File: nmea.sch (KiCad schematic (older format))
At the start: 24 parts, among them P7 CONN_01X20, U7 MCP2562, U8 SN65C1168E, U9 INA219

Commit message: More renaming from bb to kbox
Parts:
- P7: footprint bb:TerminalBlock_Pheonix_PT-3.5mm_20pol -> kbox:TerminalBlock_Pheonix_PT-3.5mm_20pol
- U7, U9: footprint bb:SOIC8N -> kbox:SOIC8N
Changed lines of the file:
@@
 EESchema Schematic File Version 2
-LIBS:bb
+LIBS:kbox
 LIBS:power
 LIBS:device
@@
 LIBS:w_device
 LIBS:gsg-symbols
-LIBS:bb1-cache
+LIBS:kbox-cache
 EELAYER 25 0
 EELAYER END
@@
 F 0 "U7" H 2900 1550 60  0000 C CNN
 F 1 "MCP2562" H 2850 2050 60  0000 C CNN
-F 2 "bb:SOIC8N" H 2900 1750 60  0001 C CNN
+F 2 "kbox:SOIC8N" H 2900 1750 60  0001 C CNN
 F 3 "" H 2900 1750 60  0000 C CNN
 F 4 "MCP2562T-E/SN" H 2900 1850 60  0001 C CNN "PartNumber"
@@
 F 0 "U9" H 3400 4950 60  0000 C CNN
 F 1 "INA219" H 3100 4950 60  0000 C CNN
-F 2 "bb:SOIC8N" H 3200 4700 60  0001 C CNN
+F 2 "kbox:SOIC8N" H 3200 4700 60  0001 C CNN
 F 3 "" H 3200 4700 60  0000 C CNN
 F 4 "INA219BIDR" H 3200 4700 60  0001 C CNN "PartNumber"
@@
 F 0 "P7" H 9350 5800 50  0000 C CNN
 F 1 "CONN_01X20" V 9450 4750 50  0000 C CNN
-F 2 "bb:TerminalBlock_Pheonix_PT-3.5mm_20pol" H 9350 4750 60  0001 C CNN
+F 2 "kbox:TerminalBlock_Pheonix_PT-3.5mm_20pol" H 9350 4750 60  0001 C CNN
 F 3 "" H 9350 4750 60  0000 C CNN
 F 4 "1709678" H 9350 4750 60  0001 C CNN "PartNumber"

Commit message: Fixing some parts numbers for pcbng import
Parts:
- R19, R21, R23: PartNumber P10KDBCT-ND -> ERA-3AEB103V
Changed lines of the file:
@@
 F 2 "Resistors_SMD:R_0603" V 2930 5650 30  0001 C CNN
 F 3 "" H 3000 5650 30  0000 C CNN
-F 4 "P10KDBCT-ND" V 3000 5650 60  0001 C CNN "PartNumber"
+F 4 "ERA-3AEB103V" V 3000 5650 60  0001 C CNN "PartNumber"
 	1    3000 5650
 	1    0    0    -1
@@
 F 2 "Resistors_SMD:R_0603" V 2930 6250 30  0001 C CNN
 F 3 "" H 3000 6250 30  0000 C CNN
-F 4 "P10KDBCT-ND" V 3000 6250 60  0001 C CNN "PartNumber"
+F 4 "ERA-3AEB103V" V 3000 6250 60  0001 C CNN "PartNumber"
 	1    3000 6250
 	1    0    0    -1
@@
 F 2 "Resistors_SMD:R_0603" V 2930 6850 30  0001 C CNN
 F 3 "" H 3000 6850 30  0000 C CNN
-F 4 "P10KDBCT-ND" V 3000 6850 60  0001 C CNN "PartNumber"
+F 4 "ERA-3AEB103V" V 3000 6850 60  0001 C CNN "PartNumber"
 	1    3000 6850
 	1    0    0    -1

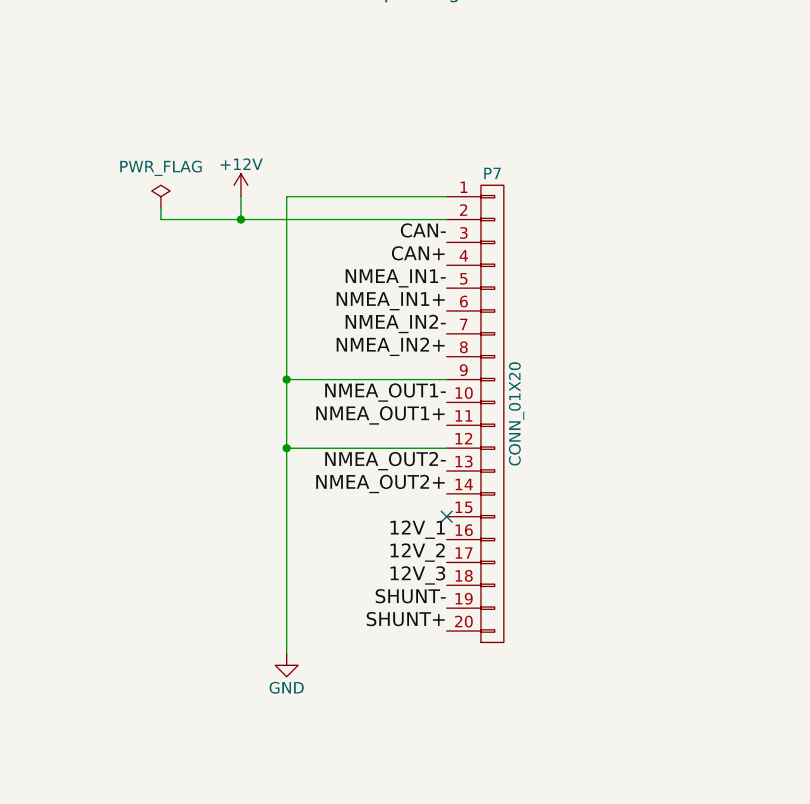
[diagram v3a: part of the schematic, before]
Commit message: Updated schematic for v1.1
 - 12V will now be measured before the input protection
 - Removed IMU_INT and IMU_EN from extension connector
 - Added +5V and +12V on extension connector
 - Removed 1 on of the two grounds included with NMEA outputs
 - Added a pulse input on the main connector, with input protection
 - Split the 20pin connector into two separate connector. Changed to a
 model that does not require a screwdriver.
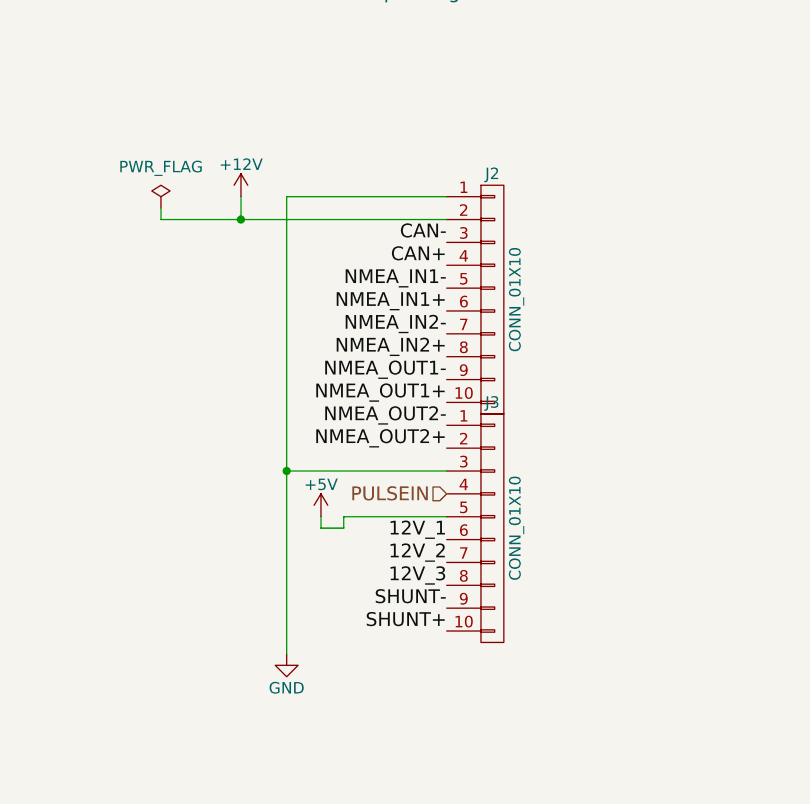
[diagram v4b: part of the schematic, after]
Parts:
- removed P7: CONN_01X20, kbox:TerminalBlock_Pheonix_PT-3.5mm_20pol, symbol CONN_01X20
- added J2, J3: CONN_01X10, TerminalBlock_Phoenix:TerminalBlock_Phoenix_PT-3.5mm_10pol, symbol CONN_01X10
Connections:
- net +12V: now also J2.2 (P2)
- net +5V: now also J3.5 (P5)
- net 12V_1: now also J3.6 (P6)
- net 12V_2: now also J3.7 (P7)
- net 12V_3: now also J3.8 (P8)
- net CAN+: now also J2.4 (P4)
- net CAN-: now also J2.3 (P3)
- net GND: now also J2.1 (P1), J3.3 (P3)
- net NMEA_IN1+: now also J2.6 (P6)
- net NMEA_IN1-: now also J2.5 (P5)
- net NMEA_IN2+: now also J2.8 (P8)
- net NMEA_IN2-: now also J2.7 (P7)
- net NMEA_OUT1+: now also J2.10 (P10)
- net NMEA_OUT1-: now also J2.9 (P9)
- net NMEA_OUT2+: now also J3.2 (P2)
- net NMEA_OUT2-: now also J3.1 (P1)
- net SHUNT+: now also J3.10 (P10)
- net SHUNT-: now also J3.9 (P9)
- new net PULSEIN: J3.4 (P4)
- no-connect marks 1 -> 0
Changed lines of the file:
@@
 $EndComp
 $Comp
-L GND #PWR049
+L GND #PWR053
 U 1 1 5660859F
 P 3250 5850
-F 0 "#PWR049" H 3250 5600 50  0001 C CNN
+F 0 "#PWR053" H 3250 5600 50  0001 C CNN
 F 1 "GND" H 3250 5700 50  0000 C CNN
 F 2 "" H 3250 5850 60  0000 C CNN
@@
 $EndComp
 $Comp
-L +3.3V #PWR050
+L +3.3V #PWR054
 U 1 1 5661817C
 P 3500 2200
-F 0 "#PWR050" H 3500 2050 50  0001 C CNN
+F 0 "#PWR054" H 3500 2050 50  0001 C CNN
 F 1 "+3.3V" H 3500 2340 50  0000 C CNN
 F 2 "" H 3500 2200 60  0000 C CNN
@@
 $EndComp
 $Comp
-L GND #PWR051
+L GND #PWR055
 U 1 1 5661CF45
 P 1900 2150
-F 0 "#PWR051" H 1900 1900 50  0001 C CNN
+F 0 "#PWR055" H 1900 1900 50  0001 C CNN
 F 1 "GND" H 1900 2000 50  0000 C CNN
 F 2 "" H 1900 2150 60  0000 C CNN
@@
 $EndComp
 $Comp
-L +5V #PWR052
+L +5V #PWR056
 U 1 1 5661EB70
 P 1600 1700
-F 0 "#PWR052" H 1600 1550 50  0001 C CNN
+F 0 "#PWR056" H 1600 1550 50  0001 C CNN
 F 1 "+5V" H 1600 1840 50  0000 C CNN
 F 2 "" H 1600 1700 60  0000 C CNN
@@
 $EndComp
 $Comp
-L GND #PWR053
+L GND #PWR057
 U 1 1 5663157A
 P 3400 2550
-F 0 "#PWR053" H 3400 2300 50  0001 C CNN
+F 0 "#PWR057" H 3400 2300 50  0001 C CNN
 F 1 "GND" H 3400 2400 50  0000 C CNN
 F 2 "" H 3400 2550 60  0000 C CNN
@@
 $EndComp
 $Comp
-L GND #PWR054
+L GND #PWR058
 U 1 1 56633AB1
 P 1600 2250
-F 0 "#PWR054" H 1600 2000 50  0001 C CNN
+F 0 "#PWR058" H 1600 2000 50  0001 C CNN
 F 1 "GND" H 1600 2100 50  0000 C CNN
 F 2 "" H 1600 2250 60  0000 C CNN
@@
 $EndComp
 $Comp
-L GND #PWR055
+L GND #PWR059
 U 1 1 5671B320
 P 3250 6450
-F 0 "#PWR055" H 3250 6200 50  0001 C CNN
+F 0 "#PWR059" H 3250 6200 50  0001 C CNN
 F 1 "GND" H 3250 6300 50  0000 C CNN
 F 2 "" H 3250 6450 60  0000 C CNN
@@
 $EndComp
 $Comp
-L GND #PWR056
+L GND #PWR060
 U 1 1 5671D29F
 P 3250 7050
-F 0 "#PWR056" H 3250 6800 50  0001 C CNN
+F 0 "#PWR060" H 3250 6800 50  0001 C CNN
 F 1 "GND" H 3250 6900 50  0000 C CNN
 F 2 "" H 3250 7050 60  0000 C CNN
@@
 ANALOG3
 $Comp
-L +12V #PWR057
+L +12V #PWR061
 U 1 1 567F4FFA
 P 8250 3800
-F 0 "#PWR057" H 8250 3650 50  0001 C CNN
+F 0 "#PWR061" H 8250 3650 50  0001 C CNN
 F 1 "+12V" H 8250 3940 50  0000 C CNN
 F 2 "" H 8250 3800 60  0000 C CNN
@@
 $EndComp
 $Comp
-L GND #PWR058
+L GND #PWR062
 U 1 1 56805BCC
 P 2250 5100
-F 0 "#PWR058" H 2250 4850 50  0001 C CNN
+F 0 "#PWR062" H 2250 4850 50  0001 C CNN
 F 1 "GND" H 2250 4950 50  0000 C CNN
 F 2 "" H 2250 5100 60  0000 C CNN
@@
 $EndComp
 $Comp
-L PWR_FLAG #FLG059
+L PWR_FLAG #FLG063
 U 1 1 568074D6
 P 7900 3850
-F 0 "#FLG059" H 7900 3945 50  0001 C CNN
+F 0 "#FLG063" H 7900 3945 50  0001 C CNN
 F 1 "PWR_FLAG" H 7900 4030 50  0000 C CNN
 F 2 "" H 7900 3850 60  0000 C CNN
@@
 $EndComp
 $Comp
-L +3.3V #PWR060
+L +3.3V #PWR064
 U 1 1 56699F39
 P 2700 4400
-F 0 "#PWR060" H 2700 4250 50  0001 C CNN
+F 0 "#PWR064" H 2700 4250 50  0001 C CNN
 F 1 "+3.3V" H 2700 4540 50  0000 C CNN
 F 2 "" H 2700 4400 60  0000 C CNN
@@
 $EndComp
 $Comp
-L GND #PWR061
+L GND #PWR065
 U 1 1 5669B7A7
 P 4500 5000
-F 0 "#PWR061" H 4500 4750 50  0001 C CNN
+F 0 "#PWR065" H 4500 4750 50  0001 C CNN
 F 1 "GND" H 4500 4850 50  0000 C CNN
 F 2 "" H 4500 5000 60  0000 C CNN
@@
 $EndComp
 $Comp
-L +5V #PWR062
+L +5V #PWR066
 U 1 1 5665D00E
 P 8450 1100
-F 0 "#PWR062" H 8450 950 50  0001 C CNN
+F 0 "#PWR066" H 8450 950 50  0001 C CNN
 F 1 "+5V" H 8450 1240 50  0000 C CNN
 F 2 "" H 8450 1100 60  0000 C CNN
@@
 $EndComp
 $Comp
-L GND #PWR063
+L GND #PWR067
 U 1 1 5665D465
 P 8650 1500
-F 0 "#PWR063" H 8650 1250 50  0001 C CNN
+F 0 "#PWR067" H 8650 1250 50  0001 C CNN
 F 1 "GND" H 8650 1350 50  0000 C CNN
 F 2 "" H 8650 1500 60  0000 C CNN
@@
 $EndComp
 $Comp
-L GND #PWR064
+L GND #PWR068
 U 1 1 566617E0
 P 7100 2600
-F 0 "#PWR064" H 7100 2350 50  0001 C CNN
+F 0 "#PWR068" H 7100 2350 50  0001 C CNN
 F 1 "GND" H 7100 2450 50  0000 C CNN
 F 2 "" H 7100 2600 60  0000 C CNN
@@
 $EndComp
 $Comp
-L GND #PWR065
+L GND #PWR069
 U 1 1 5667B0C5
 P 7800 1300
-F 0 "#PWR065" H 7800 1050 50  0001 C CNN
+F 0 "#PWR069" H 7800 1050 50  0001 C CNN
 F 1 "GND" H 7800 1150 50  0000 C CNN
 F 2 "" H 7800 1300 60  0000 C CNN
@@
 	7800 1250 7800 1300
 Connection ~ 7800 1250
-$Comp
-L CONN_01X20 P7
-U 1 1 566AE4E8
-P 9350 4750
-F 0 "P7" H 9350 5800 50  0000 C CNN
-F 1 "CONN_01X20" V 9450 4750 50  0000 C CNN
-F 2 "kbox:TerminalBlock_Pheonix_PT-3.5mm_20pol" H 9350 4750 60  0001 C CNN
-F 3 "" H 9350 4750 60  0000 C CNN
-F 4 "1709678" H 9350 4750 60  0001 C CNN "PartNumber"
-	1    9350 4750
-	1    0    0    -1
-$EndComp
 Wire Wire Line
 	3300 1850 3400 1850
@@
 Text Label 9150 4400 2    60   ~ 0
 NMEA_IN2-
-Text Label 9150 4800 2    60   ~ 0
+Text Label 9150 4700 2    60   ~ 0
 NMEA_OUT1+
-Text Label 9150 4700 2    60   ~ 0
+Text Label 9150 4600 2    60   ~ 0
 NMEA_OUT1-
-Text Label 9150 5100 2    60   ~ 0
+Text Label 9150 4900 2    60   ~ 0
 NMEA_OUT2+
-Text Label 9150 5000 2    60   ~ 0
-NMEA_OUT2-
 Text Label 9150 5300 2    60   ~ 0
 12V_1
@@
 Text Label 9150 5700 2    60   ~ 0
 SHUNT+
-NoConn ~ 9150 5200
-Wire Wire Line
-	9150 4600 8450 4600
-Wire Wire Line
-	8450 4900 9150 4900
 Wire Wire Line
 	8450 3800 8450 5800
-Connection ~ 8450 4600
-Connection ~ 8450 4900
-$Comp
-L GND #PWR066
+$Comp
+L GND #PWR070
 U 1 1 566C9EC9
 P 8450 5800
-F 0 "#PWR066" H 8450 5550 50  0001 C CNN
+F 0 "#PWR070" H 8450 5550 50  0001 C CNN
 F 1 "GND" H 8450 5650 50  0000 C CNN
 F 2 "" H 8450 5800 60  0000 C CNN
@@
 Wire Wire Line
 	6550 2050 6550 2100
+Text Label 9150 4800 2    60   ~ 0
+NMEA_OUT2-
+Wire Wire Line
+	9150 5000 8450 5000
+Connection ~ 8450 5000
+Wire Wire Line
+	8700 5200 9150 5200
+$Comp
+L +5V #PWR071
+U 1 1 5A77337A
+P 8600 5200
+F 0 "#PWR071" H 8600 5050 50  0001 C CNN
+F 1 "+5V" H 8600 5340 50  0000 C CNN
+F 2 "" H 8600 5200 60  0000 C CNN
+F 3 "" H 8600 5200 60  0000 C CNN
+	1    8600 5200
+	1    0    0    -1
+$EndComp
+Wire Wire Line
+	8700 5200 8700 5250
+Wire Wire Line
+	8700 5250 8600 5250
+Wire Wire Line
+	8600 5250 8600 5200
+$Comp
+L CONN_01X10 J2
+U 1 1 5A8D7175
+P 9350 4250
+F 0 "J2" H 9350 4800 50  0000 C CNN
+F 1 "CONN_01X10" V 9450 4250 50  0000 C CNN
+F 2 "TerminalBlock_Phoenix:TerminalBlock_Phoenix_PT-3.5mm_10pol" H 9350 4250 50  0001 C CNN
+F 3 "" H 9350 4250 50  0001 C CNN
+F 4 "277-12192-ND " H 9350 4250 60  0001 C CNN "PartNumber"
+	1    9350 4250
+	1    0    0    -1
+$EndComp
+$Comp
+L CONN_01X10 J3
+U 1 1 5A8D7221
+P 9350 5250
+F 0 "J3" H 9350 5800 50  0000 C CNN
+F 1 "CONN_01X10" V 9450 5250 50  0000 C CNN
+F 2 "TerminalBlock_Phoenix:TerminalBlock_Phoenix_PT-3.5mm_10pol" H 9350 5250 50  0001 C CNN
+F 3 "" H 9350 5250 50  0001 C CNN
+F 4 "277-12192-ND " H 9350 5250 60  0001 C CNN "PartNumber"
+	1    9350 5250
+	1    0    0    -1
+$EndComp
+Text HLabel 9150 5100 0    60   Input ~ 0
+PULSEIN
 $EndSCHEMATC

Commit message: PCB changes for kbox 1.1a
Plus a few minor part reference changes to match what is available now.
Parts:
- D7, D8, D9: PartNumber MM3Z5V1ST1G -> MM3Z5V1T1G
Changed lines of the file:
@@
 F 2 "Diodes_SMD:SOD-323" H 3250 5650 60  0001 C CNN
 F 3 "" H 3250 5650 60  0000 C CNN
-F 4 "MM3Z5V1ST1G" H 3250 5650 60  0001 C CNN "PartNumber"
+F 4 "MM3Z5V1T1G" H 3250 5650 60  0001 C CNN "PartNumber"
 	1    3250 5650
 	0    1    1    0
@@
 F 2 "Diodes_SMD:SOD-323" H 3250 6250 60  0001 C CNN
 F 3 "" H 3250 6250 60  0000 C CNN
-F 4 "MM3Z5V1ST1G" H 3250 6250 60  0001 C CNN "PartNumber"
+F 4 "MM3Z5V1T1G" H 3250 6250 60  0001 C CNN "PartNumber"
 	1    3250 6250
 	0    1    1    0
@@
 F 2 "Diodes_SMD:SOD-323" H 3250 6850 60  0001 C CNN
 F 3 "" H 3250 6850 60  0000 C CNN
-F 4 "MM3Z5V1ST1G" H 3250 6850 60  0001 C CNN "PartNumber"
+F 4 "MM3Z5V1T1G" H 3250 6850 60  0001 C CNN "PartNumber"
 	1    3250 6850
 	0    1    1    0
